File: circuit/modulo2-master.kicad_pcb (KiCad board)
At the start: 2 copper layers, 100 x 48 mm, 34 parts, among them J1 CONN_01X02, J2 CONN_01X04, J3 CONN_01X04, J4 HOLE, J5 HOLE, J6 HOLE, J7 HOLE, Q1 BC547, Q2 BC557, U1 LM358

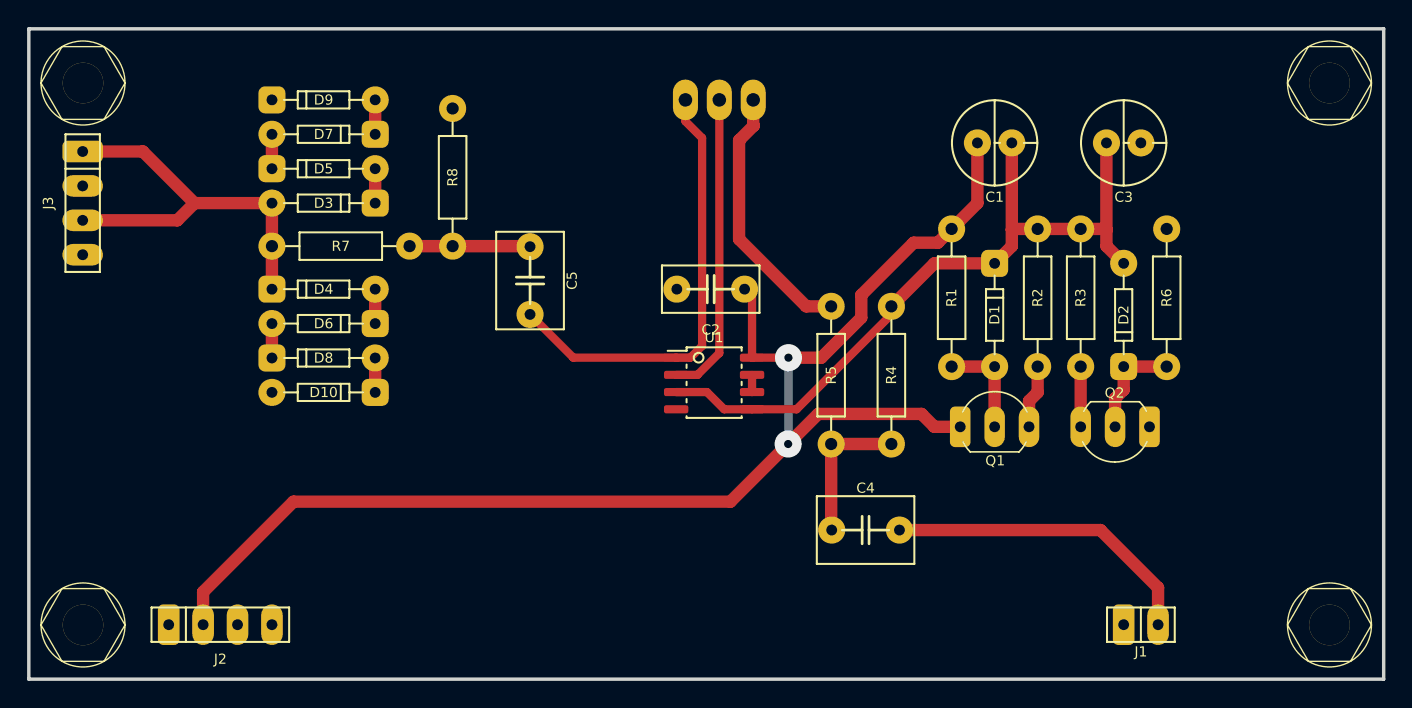
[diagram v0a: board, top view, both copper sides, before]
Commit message: master volume with TMB tone stack; fv1 initial
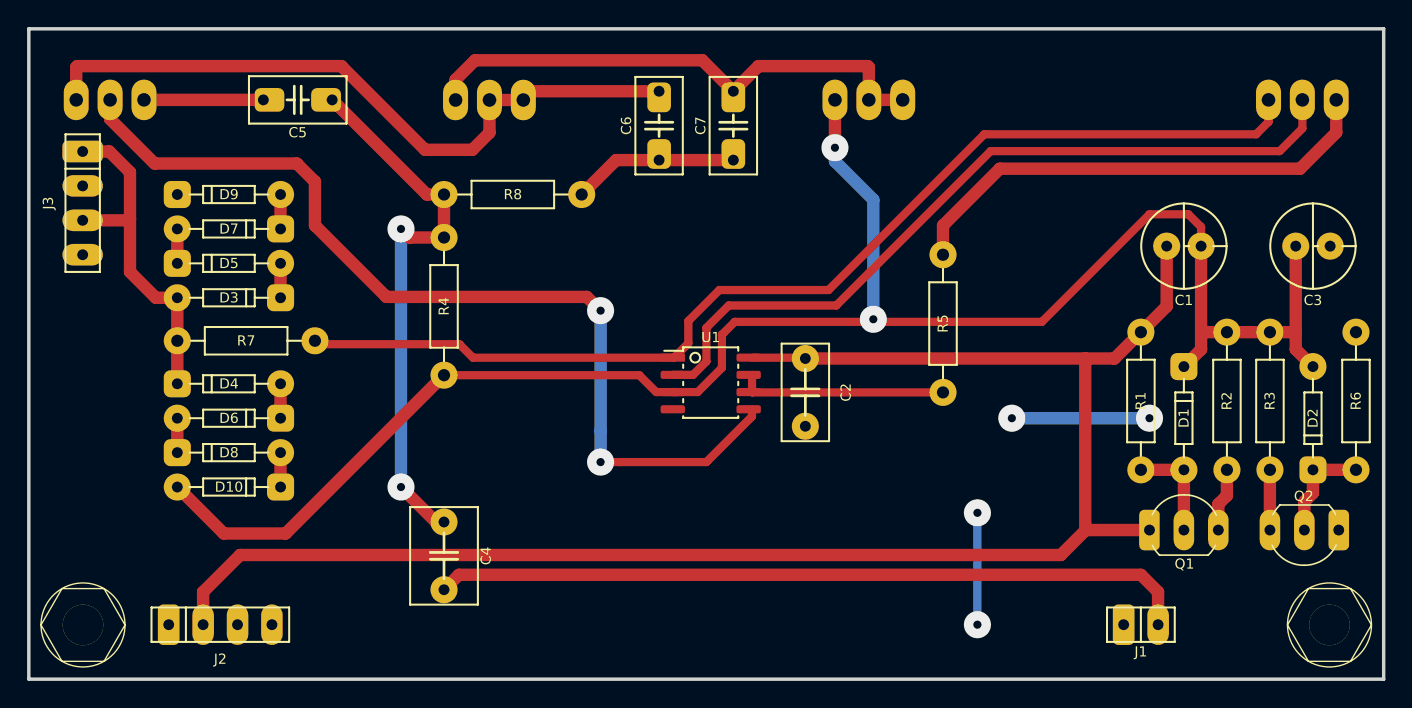
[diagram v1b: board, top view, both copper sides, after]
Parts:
- removed J4, J6: HOLE, myAmp:MountingHole
- added C6: 100nF, myAmp:C_5MM_1206, F.Cu at (96.5, 57.1)
- added C7: 47nF, myAmp:C_5MM_1206, F.Cu at (102.0, 57.1)
- added RV2: A250K, myAmp:BOURNS_PTD901_xx15K, B.Cu at (56.0, 55.2)
- added RV3: A250K, myAmp:BOURNS_PTD901_xx15K, B.Cu at (84.0, 55.3)
- added RV4: 10K, myAmp:BOURNS_PTD901_xx15K, B.Cu at (112.0, 55.2)
- C5: value 680nF -> 250pF; footprint myAmp:C_FILM_L7.2mm_W5.5mm_P5.00mm -> myAmp:C_5MM_1206
- R4: value 470k -> 1M
- R5: value 39k -> 10k
- R7: value 1k -> 47
- R8: value 470k -> 100k
- moved RV1 43.0 mm to (144.0, 55.2)
- moved R4 33.4 mm to (80.6, 70.5), turned to 90 degrees
- moved C4 31.2 mm to (80.6, 88.9), turned to 90 degrees
- moved C5 21.7 mm to (69.8, 55.2), turned to 180 degrees
- moved R1 15.9 mm to (132.1, 77.5)
- moved R2 15.9 mm to (138.4, 77.5)
- moved C1 15.9 mm to (135.3, 66.0)
- moved C3 15.9 mm to (144.8, 66.0)
- moved Q1 15.9 mm to (135.3, 87.0)
- moved Q2 15.9 mm to (144.1, 87.0)
- moved R6 15.9 mm to (148.0, 77.5)
- moved D1 15.9 mm to (135.3, 78.7)
- moved D2 15.9 mm to (144.8, 78.7)
- moved R3 15.9 mm to (141.6, 77.5)
- moved C2 10.3 mm to (107.3, 76.8), turned to 90 degrees
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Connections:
- C5 pad 1: Net-(C5-Pad1) -> Net-(C4-Pad2)
- D10 pad 2: GND -> /VGND
- D9 pad 1: GND -> /VGND
- R5 pad 1: Net-(C4-Pad2) -> Net-(R5-Pad1)
- R7 pad 1: Net-(C5-Pad2) -> Net-(R7-Pad1)
- R8 pad 1: Net-(C5-Pad2) -> Net-(C6-Pad1)
- R8 pad 2: GND -> Net-(C4-Pad2)
- RV1 pad 1: Net-(C5-Pad1) -> Net-(R7-Pad1)
- U1 pad 1: Net-(C5-Pad1) -> Net-(R7-Pad1)
- U1 pad 5: /VGND -> Net-(RV2-Pad2)
- U1 pad 6: Net-(U1-Pad6) -> Net-(R5-Pad1)
- U1 pad 7: Net-(U1-Pad6) -> Net-(R5-Pad1)
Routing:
- net Net-(R7-Pad1): track 0.00 -> 80.7 mm
- net /VGND: track 54.7 -> 134.5 mm, vias 0 -> 2
- net Net-(RV2-Pad2): track 0.00 -> 69.6 mm, vias 0 -> 2
- net Net-(C6-Pad2): track 0.00 -> 51.2 mm
- net Net-(C7-Pad2): track 0.00 -> 39.3 mm
- net Net-(RV1-Pad2): track 22.5 -> 57.6 mm
- net Net-(C5-Pad1): track 33.1 -> 0.00 mm
- net /in: track 23.6 -> 56.1 mm
- net Net-(C4-Pad2): track 10.8 -> 41.1 mm, vias 0 -> 2
- net +24V: track 102.6 -> 123.5 mm, vias 2 -> 0
- net GND: track 0.00 -> 18.4 mm, vias 0 -> 4
- net Net-(R5-Pad2): track 19.6 -> 36.4 mm
- net Net-(R5-Pad1): track 0.00 -> 15.4 mm
- net Net-(C6-Pad1): track 0.00 -> 12.2 mm
- net /out: track 30.7 -> 25.7 mm
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
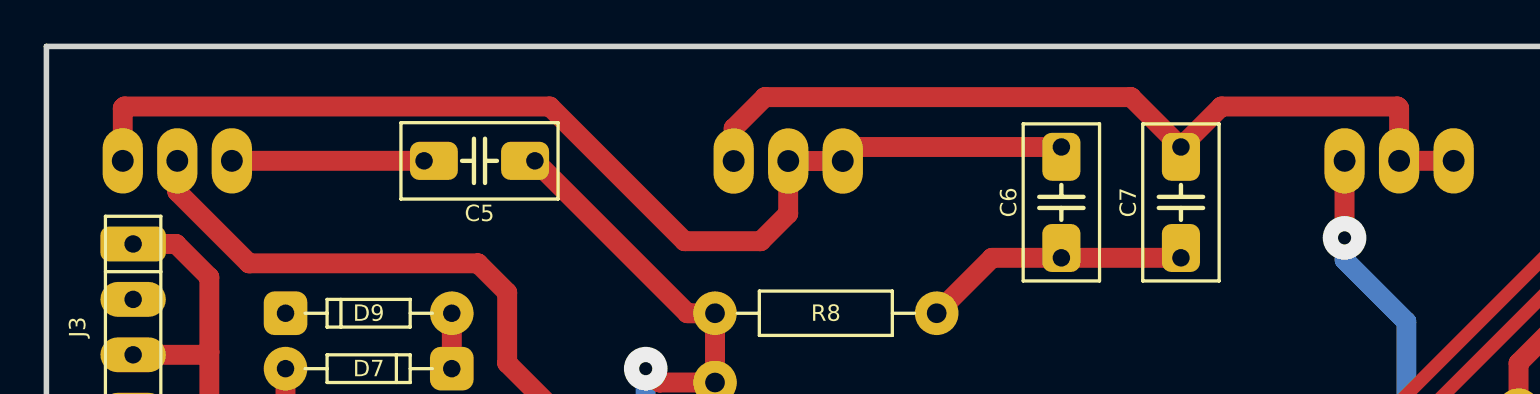
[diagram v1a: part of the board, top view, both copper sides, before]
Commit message: cleanup the the power amp a bit; still need to move the diff inputs
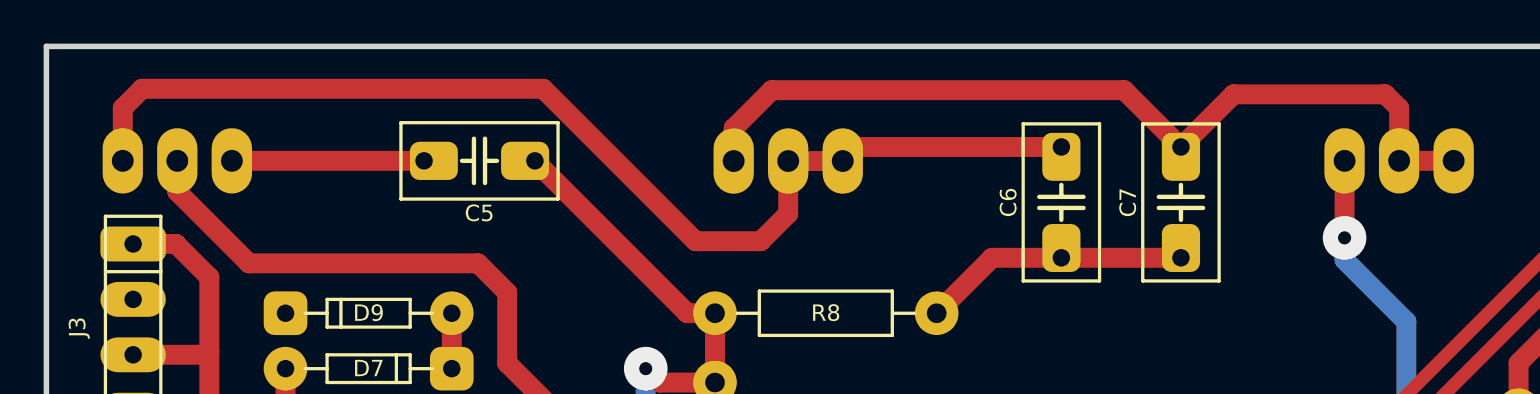
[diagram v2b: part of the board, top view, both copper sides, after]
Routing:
- net Net-(C7-Pad2): track 39.3 -> 40.0 mm
- net Net-(C6-Pad2): track 51.2 -> 51.9 mm

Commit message: master done (hopefully...)
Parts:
- added SW1: SW_SRC, myAmp:ESP2010_switch, F.Cu at (111.8, 94.0)
- J1: value CONN_01X02 -> CONN_01X03; footprint myAmp:PIN_1x02 -> myAmp:PIN_1x03
- moved C1 1.91 mm to (133.3, 66.0)
- moved D1 1.91 mm to (133.3, 78.7)
- moved Q1 1.91 mm to (133.3, 87.0)
- moved R1 1.91 mm to (130.2, 77.5)
- moved R2 1.91 mm to (136.5, 77.5)
- moved J1 1.27 mm to (133.3, 94.0)
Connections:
- J1 pad 2: /in -> Net-(J1-Pad2)
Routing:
- net /VGND: track 134.5 -> 163.6 mm
- net Net-(J1-Pad2): track 0.00 -> 27.3 mm
- net Net-(J1-Pad3): track 0.00 -> 26.8 mm
- net /in: track 56.1 -> 34.2 mm
- net GND: track 18.4 -> 15.9 mm, vias 4 -> 3
- net +24V: track 123.5 -> 121.9 mm
- net Net-(C7-Pad2): track 40.0 -> 38.6 mm
- net Net-(R5-Pad1): track 15.4 -> 16.7 mm
- net /out: track 25.7 -> 26.6 mm
- net Net-(C5-Pad2): track 8.81 -> 9.65 mm
- net Net-(C6-Pad2): track 51.9 -> 51.2 mm
- net Net-(RV1-Pad2): track 57.6 -> 56.9 mm
- net Net-(R5-Pad2): track 36.4 -> 35.9 mm
- net Net-(C4-Pad2): track 41.1 -> 41.6 mm

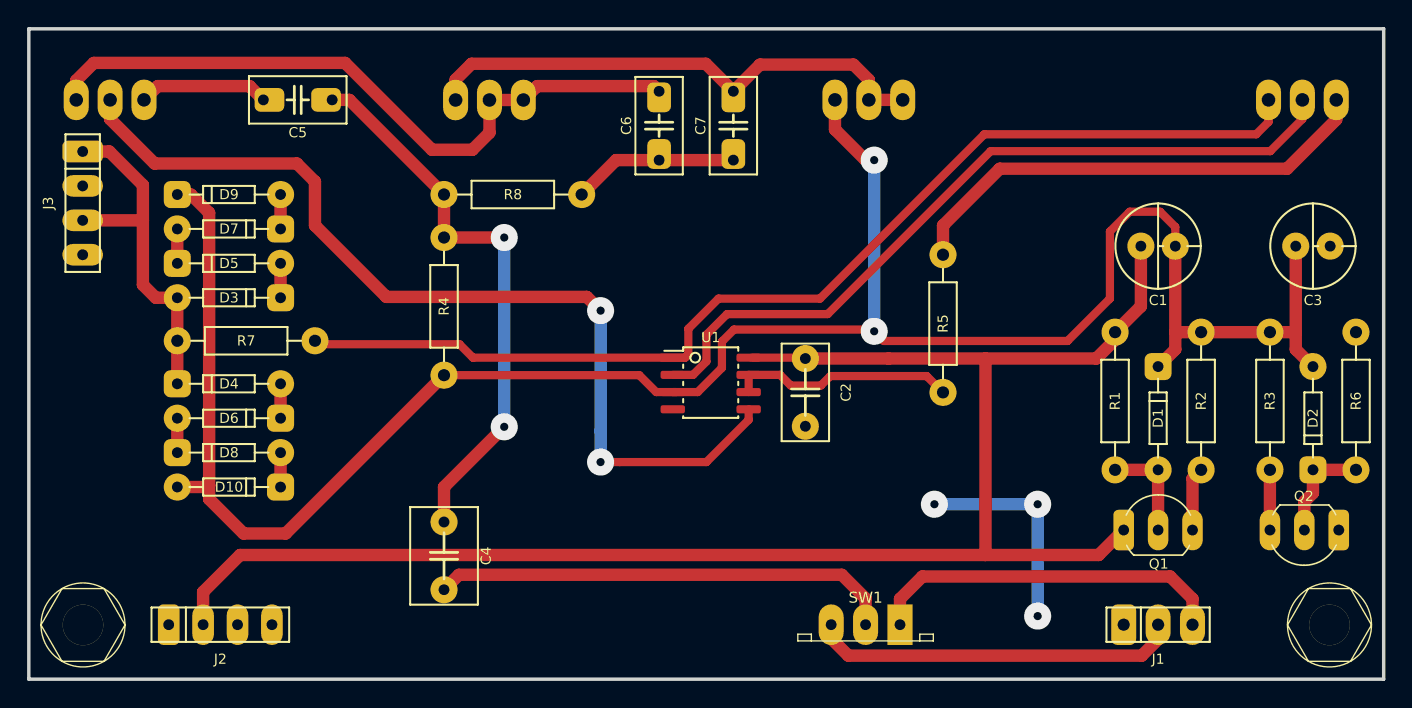
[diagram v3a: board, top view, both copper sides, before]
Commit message: master moved to kicad 6 (yikes!)
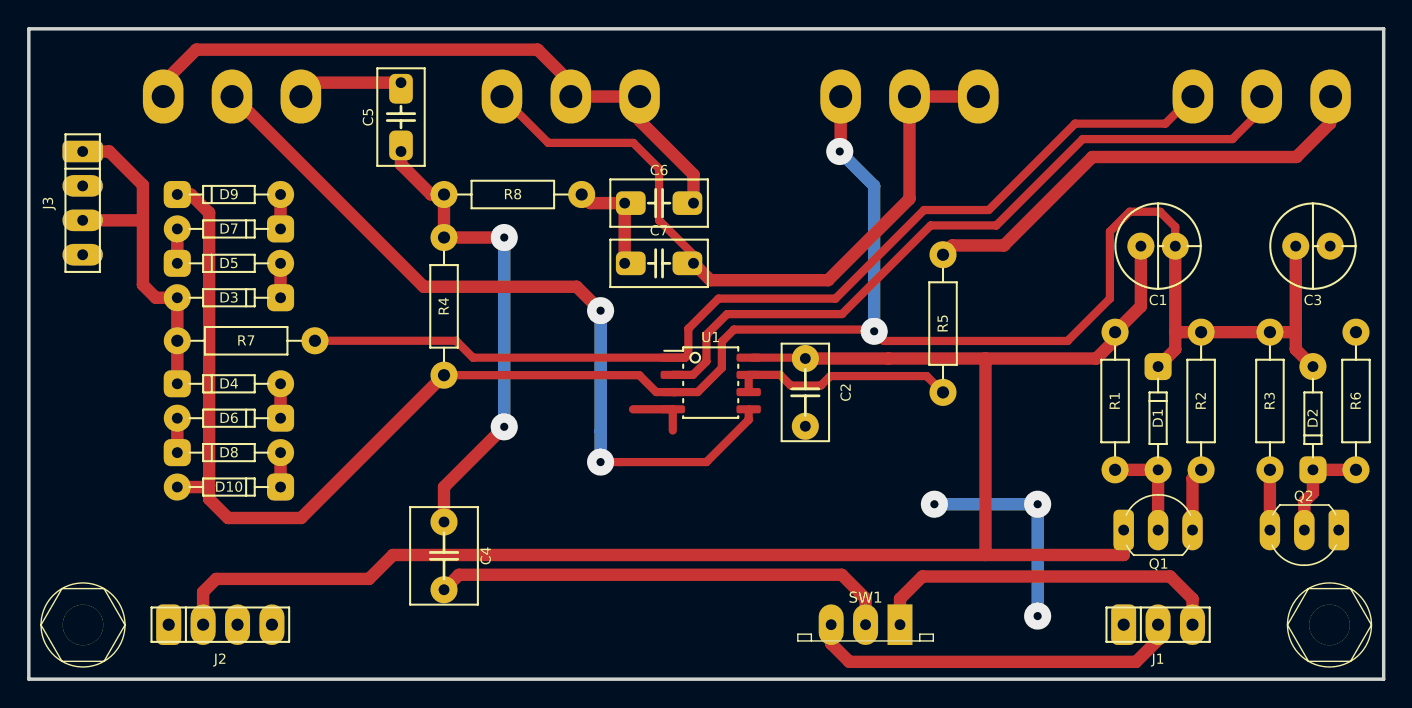
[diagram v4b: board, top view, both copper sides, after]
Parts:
- RV1: value 50K -> R_POT; footprint myAmp:BOURNS_PTD901_xx15K -> myAmp:POT_VULGARIS
- RV2, RV3, RV4: footprint myAmp:BOURNS_PTD901_xx15K -> myAmp:POT_VULGARIS
- moved C7 11.5 mm to (96.5, 67.3), turned to 0 degrees
- moved RV2 9.00 mm to (65.0, 55.0)
- moved C5 7.73 mm to (77.5, 56.5), turned to 90 degrees
- moved RV3 6.01 mm to (90.0, 55.0)
- moved C6 5.72 mm to (96.5, 62.9), turned to 0 degrees
- moved RV1 3.01 mm to (141.0, 55.0)
- moved RV4 3.01 mm to (115.0, 55.0)
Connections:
- J2 pad 3: (no net) -> unconnected-(J2-Pad3)
- J2 pad 4: (no net) -> unconnected-(J2-Pad4)
- J5 pad 1: (no net) -> unconnected-(J5-Pad1)
- J7 pad 1: (no net) -> unconnected-(J7-Pad1)
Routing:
- net Net-(C7-Pad2): track 38.6 -> 53.4 mm
- net Net-(RV2-Pad2): track 69.5 -> 58.0 mm
- net Net-(R7-Pad1): track 80.8 -> 74.4 mm
- net Net-(C4-Pad2): track 41.6 -> 35.5 mm
- net GND: track 15.9 -> 20.4 mm
- net Net-(C6-Pad2): track 51.2 -> 46.7 mm
- net Net-(C6-Pad1): track 12.2 -> 7.88 mm
- net Net-(RV1-Pad2): track 56.9 -> 53.7 mm
- net Net-(C5-Pad2): track 9.65 -> 7.39 mm
- net /VGND: track 163.6 -> 161.7 mm
- net Net-(R5-Pad2): track 35.9 -> 34.6 mm
- net +24V: track 121.9 -> 122.9 mm
- net Net-(J1-Pad2): track 27.3 -> 27.9 mm
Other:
- net class Default removed

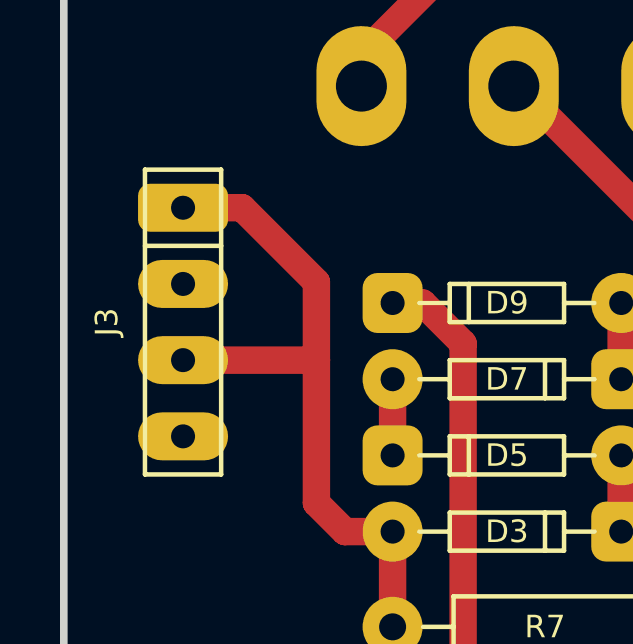
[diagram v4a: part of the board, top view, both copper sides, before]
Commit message: added new preamp sim
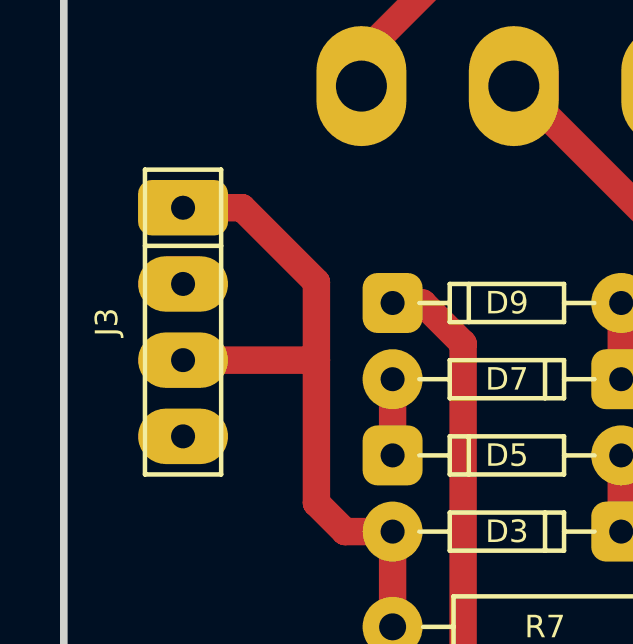
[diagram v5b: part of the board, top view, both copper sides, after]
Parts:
- C5: value 250pF -> 100pF
- C6: value 100nF -> 22nF
- RV1: value R_POT -> 5k
- RV2, RV3: value A250K -> 1M
- RV4: value 10K -> A5K
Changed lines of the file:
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@@
     (fp_line (start 5.08 -1.27) (end 5.08 1.27) (layer "F.SilkS") (width 0.15))
     (fp_line (start -5.08 -1.27) (end 5.08 -1.27) (layer "F.SilkS") (width 0.15))
-    (pad "1" thru_hole roundrect locked (at -3.81 0 270) (size 1.6 3) (drill 0.8) (layers *.Cu *.Mask) (roundrect_rratio 0.25)
+    (pad "1" thru_hole roundrect locked (at -3.81 0 270) (size 1.85 3) (drill 0.8) (layers *.Cu *.Mask) (roundrect_rratio 0.25)
       (net 17 "/out") (pinfunction "P1") (pintype "passive"))
-    (pad "2" thru_hole oval locked (at -1.27 0 270) (size 1.6 3) (drill 0.8) (layers *.Cu *.Mask)
+    (pad "2" thru_hole oval locked (at -1.27 0 270) (size 1.85 3) (drill 0.8) (layers *.Cu *.Mask)
       (net 2 "GND") (pinfunction "P2") (pintype "passive"))
-    (pad "3" thru_hole oval locked (at 1.27 0 270) (size 1.6 3) (drill 0.8) (layers *.Cu *.Mask)
+    (pad "3" thru_hole oval locked (at 1.27 0 270) (size 1.85 3) (drill 0.8) (layers *.Cu *.Mask)
       (net 17 "/out") (pintype "passive"))
-    (pad "4" thru_hole oval locked (at 3.81 0 270) (size 1.6 3) (drill 0.8) (layers *.Cu *.Mask)
+    (pad "4" thru_hole oval locked (at 3.81 0 270) (size 1.85 3) (drill 0.8) (layers *.Cu *.Mask)
       (net 2 "GND") (pintype "passive"))
     (model "${KIPRJMOD}/myAmp.pretty/models/PinHeader_1x04_P2.54mm_Vertical.step"
@@
       (effects (font (size 0.75 0.75) (thickness 0.15)))
     )
-    (fp_text value "250pF" (at -1.016 -0.254 90) (layer "F.Fab") hide
+    (fp_text value "100pF" (at -1.016 -0.254 90) (layer "F.Fab") hide
       (effects (font (size 0.127 0.127) (thickness 0.001)))
     )
@@
       (effects (font (size 0.75 0.75) (thickness 0.15)))
     )
-    (fp_text value "100nF" (at -1.016 -0.254) (layer "F.Fab") hide
+    (fp_text value "22nF" (at -1.016 -0.254) (layer "F.Fab") hide
       (effects (font (size 0.127 0.127) (thickness 0.001)))
     )
@@
       (effects (font (size 0.75 0.75) (thickness 0.15)) (justify mirror))
     )
-    (fp_text value "A250K" (at -1.27 1.905) (layer "B.Fab") hide
+    (fp_text value "1M" (at -1.27 1.905) (layer "B.Fab") hide
       (effects (font (size 0.0254 0.0254) (thickness 0.00635)) (justify mirror))
     )
@@
       (effects (font (size 0.75 0.75) (thickness 0.15)) (justify mirror))
     )
-    (fp_text value "A250K" (at -1.27 1.905) (layer "B.Fab") hide
+    (fp_text value "1M" (at -1.27 1.905) (layer "B.Fab") hide
       (effects (font (size 0.0254 0.0254) (thickness 0.00635)) (justify mirror))
     )
@@
       (effects (font (size 0.75 0.75) (thickness 0.15)) (justify mirror))
     )
-    (fp_text value "10K" (at -1.27 1.905) (layer "B.Fab") hide
+    (fp_text value "A5K" (at -1.27 1.905) (layer "B.Fab") hide
       (effects (font (size 0.0254 0.0254) (thickness 0.00635)) (justify mirror))
     )
@@
       (effects (font (size 0.75 0.75) (thickness 0.15)) (justify mirror))
     )
-    (fp_text value "R_POT" (at -1.27 1.905) (layer "B.Fab") hide
+    (fp_text value "5k" (at -1.27 1.905) (layer "B.Fab") hide
       (effects (font (size 0.0254 0.0254) (thickness 0.00635)) (justify mirror))
     )
